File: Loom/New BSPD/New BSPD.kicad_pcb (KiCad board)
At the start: 2 copper layers, 46 parts, among them J1 Conn_01x03, J2 Conn_01x03, J3 Conn_01x03, J4 Screw_Terminal_01x02, K1 MCCMA51-S-DC12V-C, Q1 IRLZ44Z, U1 4011, U10 LM2901, U11 4012, U12 74LS573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

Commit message: Fix bug in state machine counters
Realised that the reset counter would count even in an error
condition, meaning that if 10 seconds pass after shutdown, it will
turn back on instantly after the system is ok.

Fixed by making the reset counter only count if system_ok is high
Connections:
- U1 pad 11: (no net) -> Net-(U1-Pad11)
- U1 pad 12: (no net) -> /System_OK
- U1 pad 13: (no net) -> /State Machine/State_B
- U3 pad 11: (no net) -> Net-(U3-Pad11)
- U3 pad 12: (no net) -> Net-(U1-Pad11)
- U3 pad 13: (no net) -> Net-(U1-Pad11)
- U3 pad 6: /State Machine/State_B -> Net-(U3-Pad11)
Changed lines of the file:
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@@
   (net 112 "unconnected-(U15-Q7-Pad13)")
   (net 113 "unconnected-(U15-Q10-Pad15)")
+  (net 114 "Net-(U1-Pad11)")
+  (net 115 "Net-(U3-Pad11)")
   (footprint "LED_THT:LED_D5.0mm" (layer "F.Cu")
     (at 133.39 80.715)
@@
       (net 38 "Net-(U3-Pad3)") (pintype "input"))
     (pad "6" thru_hole oval (at 0 12.7) (size 1.6 1.6) (drill 0.8) (layers "*.Cu" "*.Mask")
-      (net 40 "/State Machine/State_B") (pintype "input"))
+      (net 115 "Net-(U3-Pad11)") (pintype "input"))
     (pad "7" thru_hole oval (at 0 15.24) (size 1.6 1.6) (drill 0.8) (layers "*.Cu" "*.Mask")
       (net 5 "GND") (pinfunction "VSS") (pintype "power_in"))
@@
     (pad "10" thru_hole oval (at 7.62 10.16) (size 1.6 1.6) (drill 0.8) (layers "*.Cu" "*.Mask")
       (net 41 "/State Machine/Timers/Reset_Counting") (pintype "output"))
-    (pad "11" thru_hole oval (at 7.62 7.62) (size 1.6 1.6) (drill 0.8) (layers "*.Cu" "*.Mask"))
-    (pad "12" thru_hole oval (at 7.62 5.08) (size 1.6 1.6) (drill 0.8) (layers "*.Cu" "*.Mask"))
-    (pad "13" thru_hole oval (at 7.62 2.54) (size 1.6 1.6) (drill 0.8) (layers "*.Cu" "*.Mask"))
+    (pad "11" thru_hole oval (at 7.62 7.62) (size 1.6 1.6) (drill 0.8) (layers "*.Cu" "*.Mask")
+      (net 115 "Net-(U3-Pad11)") (pintype "output"))
+    (pad "12" thru_hole oval (at 7.62 5.08) (size 1.6 1.6) (drill 0.8) (layers "*.Cu" "*.Mask")
+      (net 114 "Net-(U1-Pad11)") (pintype "input"))
+    (pad "13" thru_hole oval (at 7.62 2.54) (size 1.6 1.6) (drill 0.8) (layers "*.Cu" "*.Mask")
+      (net 114 "Net-(U1-Pad11)") (pintype "input"))
     (pad "14" thru_hole oval (at 7.62 0) (size 1.6 1.6) (drill 0.8) (layers "*.Cu" "*.Mask")
       (net 1 "+5V") (pinfunction "VDD") (pintype "power_in"))
@@
     (pad "10" thru_hole oval (at 7.62 10.16) (size 1.6 1.6) (drill 0.8) (layers "*.Cu" "*.Mask")
       (net 33 "/System_OK") (pintype "output"))
-    (pad "11" thru_hole oval (at 7.62 7.62) (size 1.6 1.6) (drill 0.8) (layers "*.Cu" "*.Mask"))
-    (pad "12" thru_hole oval (at 7.62 5.08) (size 1.6 1.6) (drill 0.8) (layers "*.Cu" "*.Mask"))
-    (pad "13" thru_hole oval (at 7.62 2.54) (size 1.6 1.6) (drill 0.8) (layers "*.Cu" "*.Mask"))
+    (pad "11" thru_hole oval (at 7.62 7.62) (size 1.6 1.6) (drill 0.8) (layers "*.Cu" "*.Mask")
+      (net 114 "Net-(U1-Pad11)") (pintype "output"))
+    (pad "12" thru_hole oval (at 7.62 5.08) (size 1.6 1.6) (drill 0.8) (layers "*.Cu" "*.Mask")
+      (net 33 "/System_OK") (pintype "input"))
+    (pad "13" thru_hole oval (at 7.62 2.54) (size 1.6 1.6) (drill 0.8) (layers "*.Cu" "*.Mask")
+      (net 40 "/State Machine/State_B") (pintype "input"))
     (pad "14" thru_hole oval (at 7.62 0) (size 1.6 1.6) (drill 0.8) (layers "*.Cu" "*.Mask")
       (net 1 "+5V") (pinfunction "VDD") (pintype "power_in"))

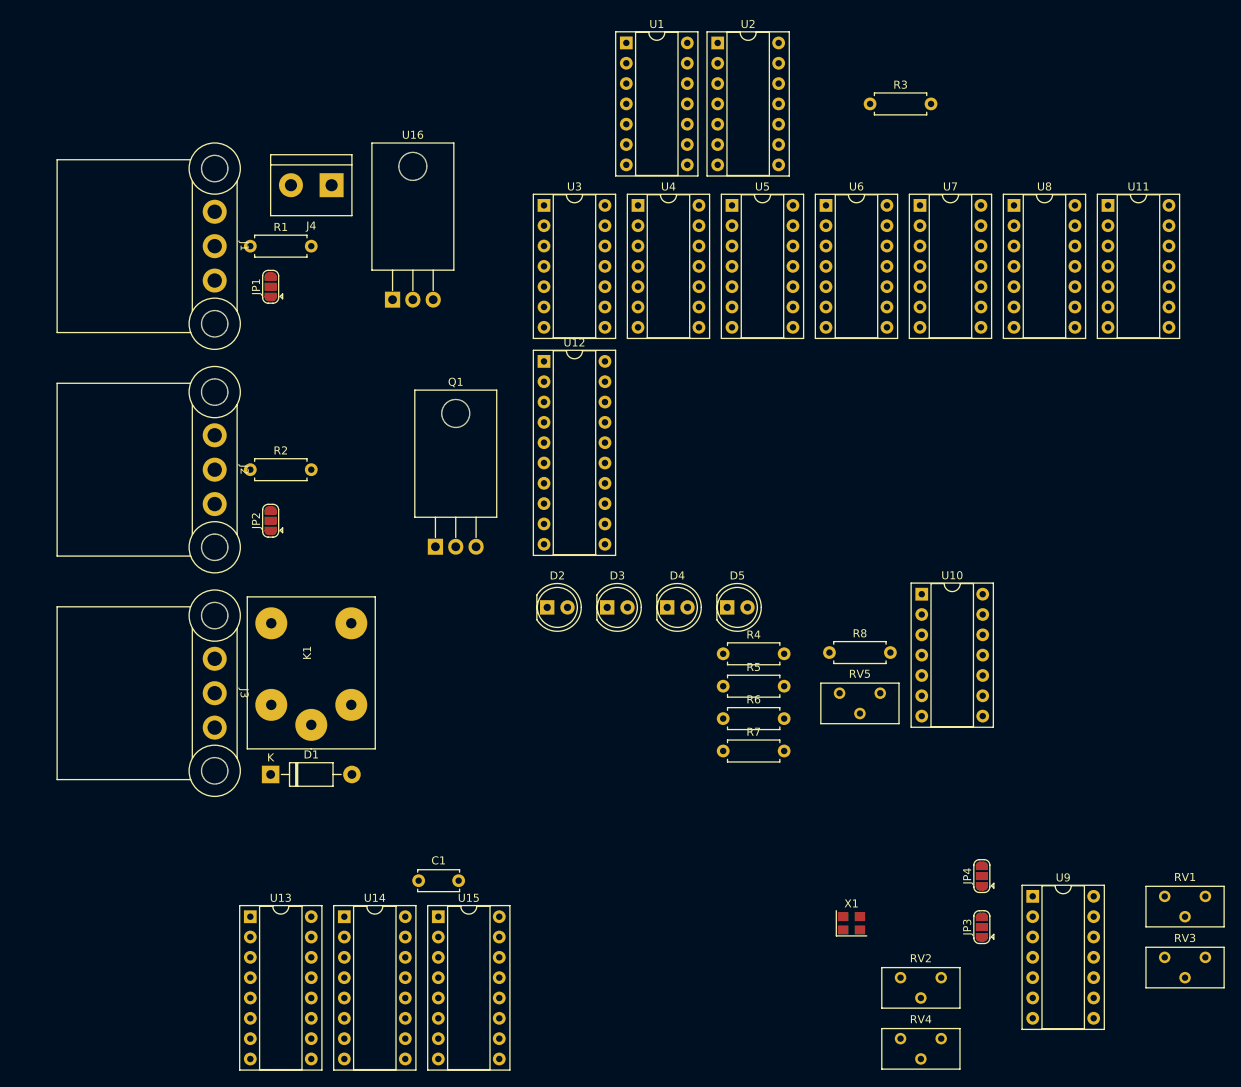
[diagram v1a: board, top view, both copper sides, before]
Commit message: Add State, Shutdown LEDs, Complete rough board layout
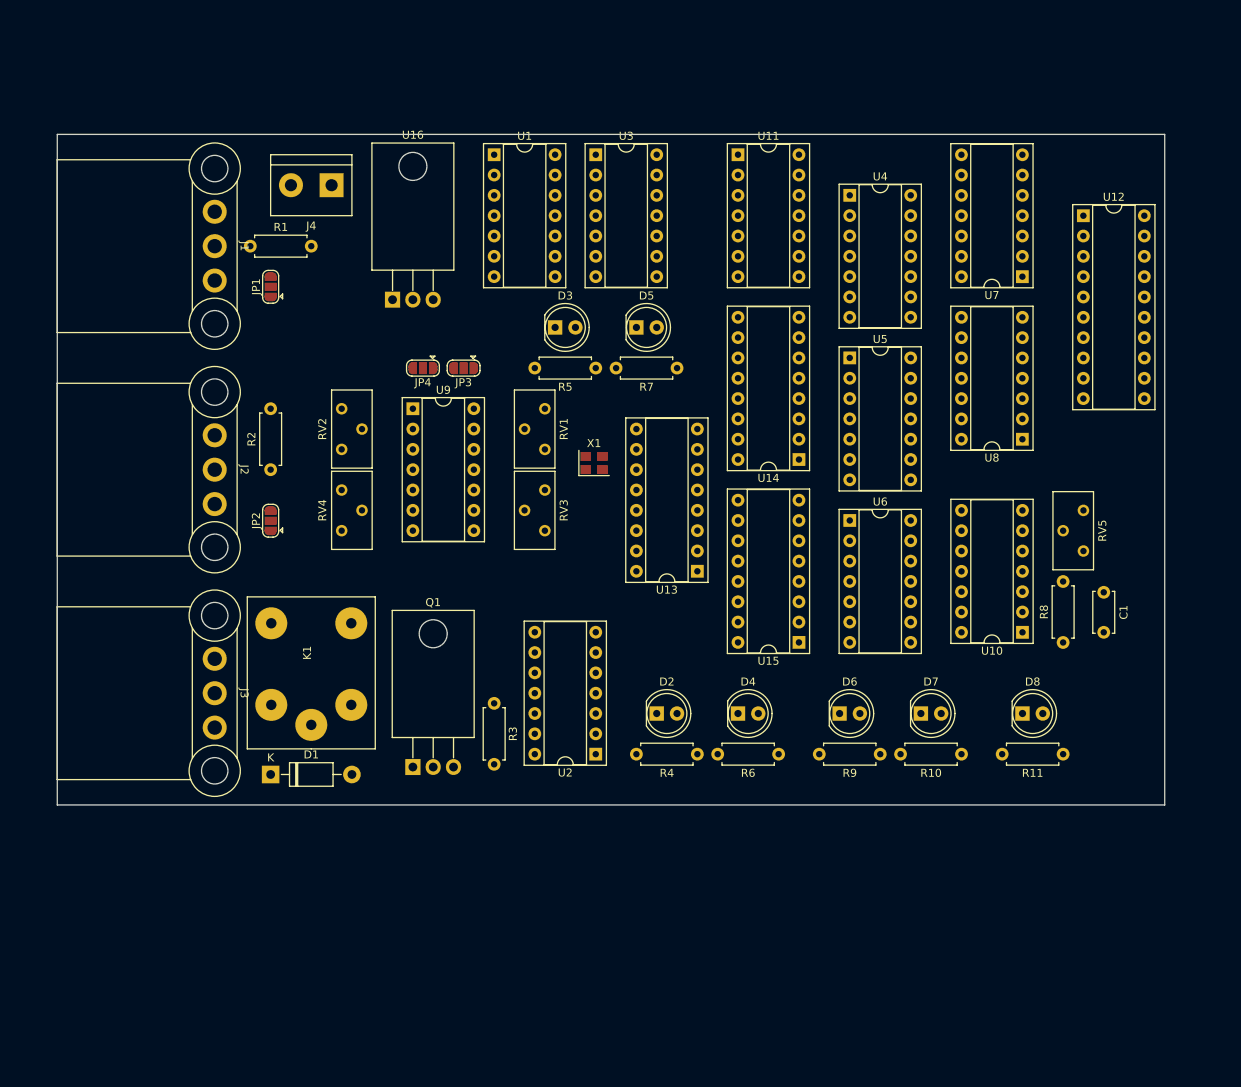
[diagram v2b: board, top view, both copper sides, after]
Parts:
- added D6: LED, LED_THT:LED_D5.0mm, F.Cu at (154.9, 94.0)
- added D7: LED, LED_THT:LED_D5.0mm, F.Cu at (165.1, 94.0)
- added D8: LED, LED_THT:LED_D5.0mm, F.Cu at (177.8, 94.0)
- added R10: 220R, Resistor_THT:R_Axial_DIN0207_L6.3mm_D2.5mm_P7.62mm_Horizontal, F.Cu at (170.2, 99.1)
- added R11: 220R, Resistor_THT:R_Axial_DIN0207_L6.3mm_D2.5mm_P7.62mm_Horizontal, F.Cu at (182.9, 99.1)
- added R9: 220R, Resistor_THT:R_Axial_DIN0207_L6.3mm_D2.5mm_P7.62mm_Horizontal, F.Cu at (160.0, 99.1)
- moved RV2 103.3 mm to (92.7, 55.9), turned to 90 degrees
- moved RV4 101.6 mm to (92.7, 66.0), turned to 90 degrees
- moved RV1 99.7 mm to (118.1, 61.0), turned to -90 degrees
- moved U9 98.6 mm to (101.6, 55.9)
- moved RV3 98.3 mm to (118.1, 71.1), turned to -90 degrees
- moved JP3 95.3 mm to (107.9, 50.8), turned to 180 degrees
- moved JP4 94.4 mm to (102.9, 50.8), turned to 180 degrees
- moved C1 92.9 mm to (188.0, 78.8), turned to -90 degrees
- moved U2 90.2 mm to (124.5, 99.1), turned to 180 degrees
- moved R3 88.4 mm to (111.8, 92.7), turned to -90 degrees
- moved U14 80.6 mm to (149.9, 62.2), turned to 180 degrees
- moved U13 70.6 mm to (137.2, 76.2), turned to 180 degrees
- moved U12 69.8 mm to (185.4, 31.8)
- moved X1 65.9 mm to (124.2, 62.7)
- moved U15 56.6 mm to (149.9, 85.1), turned to 180 degrees
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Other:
- board outline added: 138.4 x 83.8 mm

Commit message: Complete New BSPD!
TODO: Decide if the crystal needs a capacitor or not
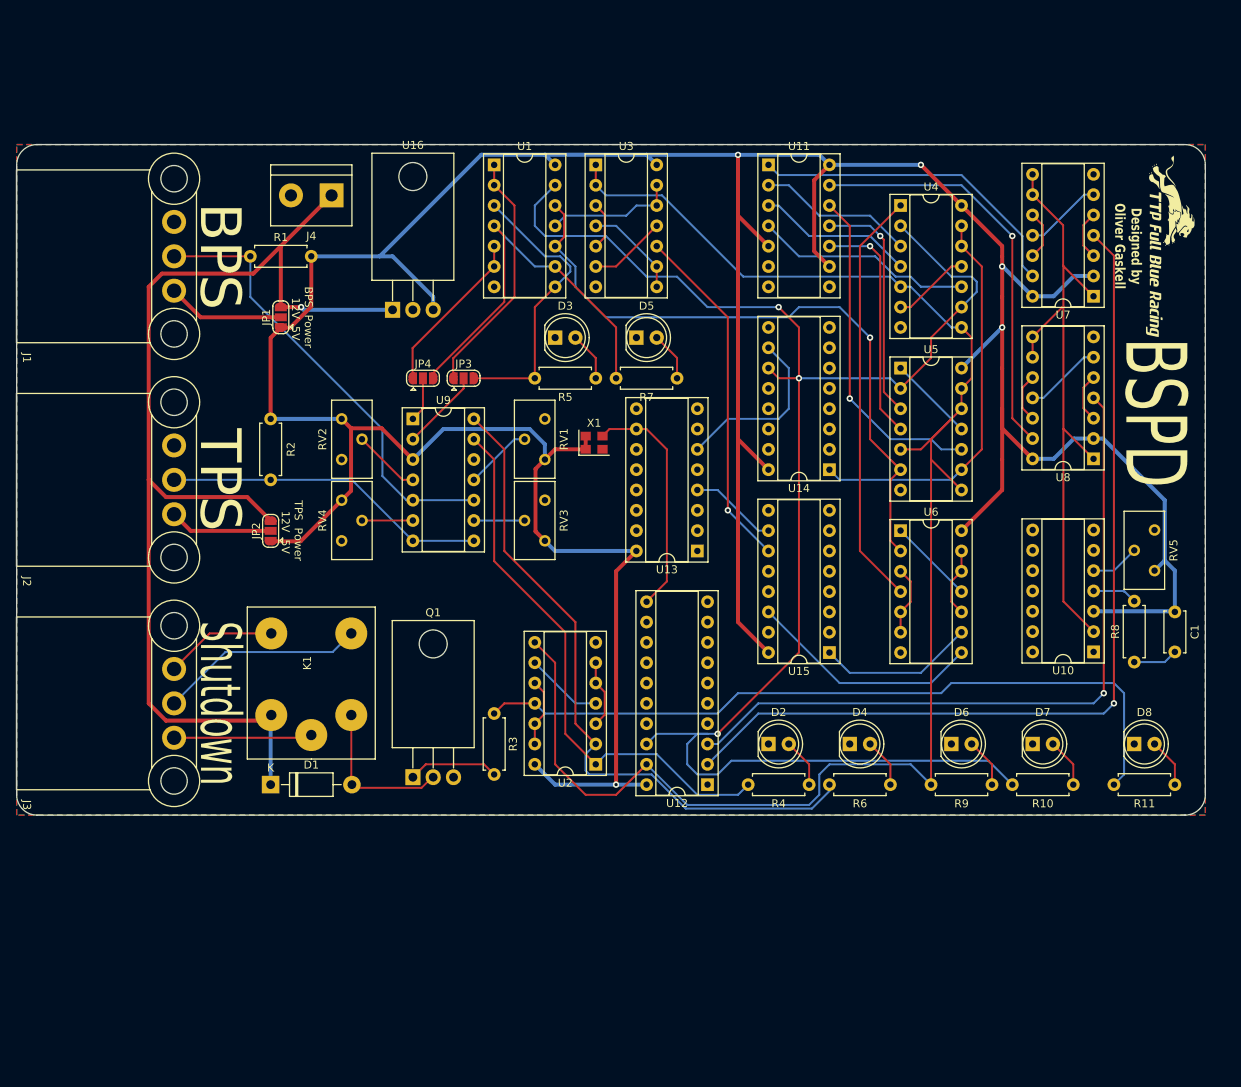
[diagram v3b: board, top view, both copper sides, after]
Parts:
- added G***: LOGO, BSPD_footprints:FBR_Logo_.9in, F.Cu at (196.8, 35.6)
- moved U12 85.2 mm to (138.4, 102.9), turned to 180 degrees
- moved D2 14.5 mm to (146.1, 97.8)
- moved D4 14.5 mm to (156.2, 97.8)
- moved D6 14.5 mm to (168.9, 97.8)
- moved D7 14.5 mm to (179.1, 97.8)
- moved D8 14.5 mm to (191.8, 97.8)
- moved R10 14.5 mm to (184.2, 102.9)
- moved R11 14.5 mm to (196.8, 102.9)
- moved R4 14.5 mm to (151.1, 102.9)
- moved R6 14.5 mm to (161.3, 102.9)
- moved R9 14.5 mm to (174.0, 102.9)
- moved R8 9.22 mm to (191.8, 87.5)
- moved RV5 9.22 mm to (194.3, 76.1)
- moved U7 9.22 mm to (186.7, 41.8)
- moved U8 9.22 mm to (186.7, 62.1)
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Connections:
- U5 pad 3: Net-(U11-Pad10) -> Net-(U11-Pad11)
- U5 pad 4: Net-(U11-Pad11) -> Net-(U11-Pad10)
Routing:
- net +5V: track 0.00 -> 474.3 mm, vias 0 -> 5
- net /State Machine/State_B: track 0.00 -> 204.8 mm, vias 0 -> 3
- net /SM_Ok: track 0.00 -> 201.9 mm
- net +12V: track 0.00 -> 144.5 mm, vias 0 -> 1
- net Net-(U12-D0): track 0.00 -> 113.5 mm, vias 0 -> 1
- net /SD_Sig: track 0.00 -> 93.9 mm
- net Net-(U12-D1): track 0.00 -> 89.6 mm, vias 0 -> 1
- net /TPS_Plugged: track 0.00 -> 85.0 mm
- net /System_OK: track 0.00 -> 82.0 mm, vias 0 -> 1
- net /RST: track 0.00 -> 78.9 mm
- net /BPS_Plugged: track 0.00 -> 69.2 mm
- net /BPS_Sig: track 0.00 -> 56.5 mm
- net Net-(U4-Pad1): track 0.00 -> 52.5 mm
- net Net-(U11-Pad13): track 0.00 -> 51.9 mm, vias 0 -> 1
- net /State Machine/5T: track 0.00 -> 50.2 mm
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- added copper zone on B.Cu, net GND
- added copper zone on F.Cu, net GND
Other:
- board size 138.4 x 83.8 mm -> 148.6 x 83.8 mm
- board text added: "BPS"
- board text added: "BPS Power 12V 5V"
- board text added: "BSPD"
- board text added: "Designed by Oliver Gaskell"
- board text added: "Shutdown"
- board text added: "TPS"
- board text added: "TPS Power 12V 5V"

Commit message: Complete Silkscreen, Fix DRC errors, Misc Cleanup
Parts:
- moved J4 3.59 mm to (88.9, 26.7)
- moved JP3 2.58 mm to (110.5, 52.1)
- moved JP4 2.50 mm to (100.4, 52.1)
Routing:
- net /BPS_Trig: track 36.1 -> 33.5 mm
- net Net-(JP3-C): track 10.2 -> 12.5 mm
- net Net-(JP3-A): track 30.9 -> 29.1 mm
- net /TPS_Trig: track 50.1 -> 51.8 mm
- net +12V: track 144.5 -> 146.0 mm
- net /SM_Ok: track 201.9 -> 203.0 mm
- net Net-(JP4-A): track 20.7 -> 21.8 mm
- net GND: vias 0 -> 24
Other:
- board text added: "12V"
- board text added: "BPS Conn"
- board text added: "BPS Trig"
- board text added: "GND"
- board text added: "System OK"
- board text added: "TPS Conn"
- board text added: "TPS Trig"

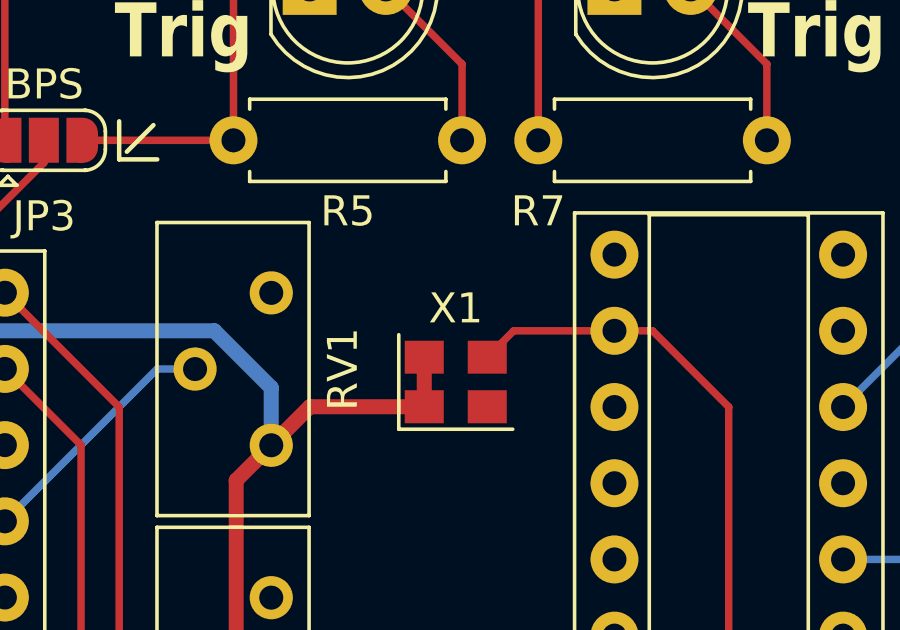
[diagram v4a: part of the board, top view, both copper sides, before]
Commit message: Add filtering capacitor for crystal power
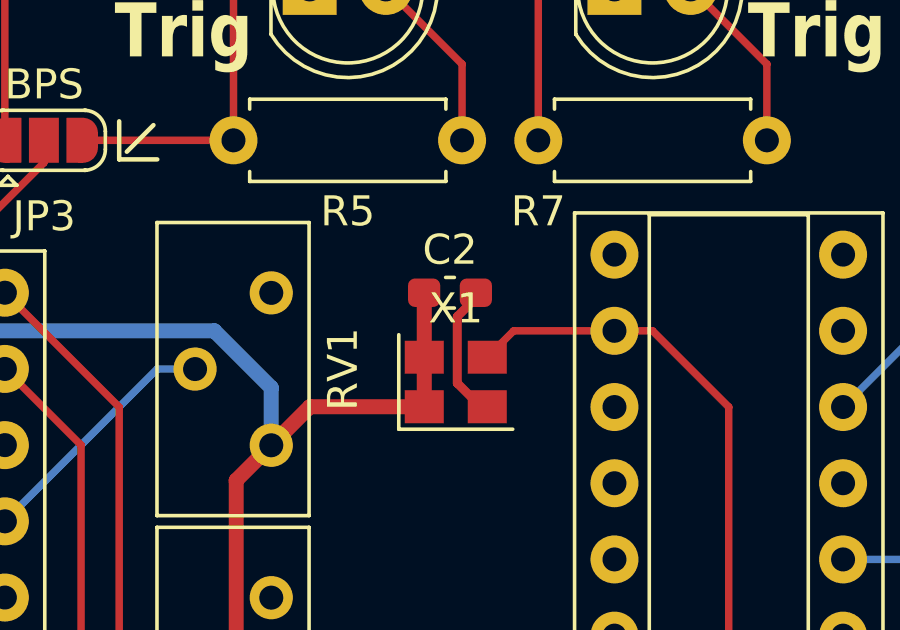
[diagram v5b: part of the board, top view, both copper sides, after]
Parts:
- added C2: 10u, Capacitor_SMD:C_0603_1608Metric_Pad1.08x0.95mm_HandSolder, F.Cu at (124.1, 57.1)
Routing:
- net GND: track 0.00 -> 4.60 mm
- net +5V: track 474.3 -> 476.5 mm
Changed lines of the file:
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@@
     )
   )
+  (footprint "Capacitor_SMD:C_0603_1608Metric_Pad1.08x0.95mm_HandSolder" (layer "F.Cu")
+    (at 124.0575 57.15)
+    (descr "Capacitor SMD 0603 (1608 Metric), square (rectangular) end terminal, IPC_7351 nominal with elongated pad for handsoldering. (Body size source: IPC-SM-782 page 76, https://www.pcb-3d.com/wordpress/wp-content/uploads/ipc-sm-782a_amendment_1_and_2.pdf), generated with kicad-footprint-generator")
+    (tags "capacitor handsolder")
+    (property "Sheetfile" "New BSPD.kicad_sch")
+    (property "Sheetname" "")
+    (property "ki_description" "Unpolarized capacitor")
+    (property "ki_keywords" "cap capacitor")
+    (attr smd)
+    (fp_text reference "C2" (at 0 -1.43) (layer "F.SilkS")
+        (effects (font (size 1 1) (thickness 0.15)))
+    )
+    (fp_text value "10u" (at 0 1.43) (layer "F.Fab")
+        (effects (font (size 1 1) (thickness 0.15)))
+    )
+    (fp_text user "${REFERENCE}" (at 0 0) (layer "F.Fab")
+        (effects (font (size 0.4 0.4) (thickness 0.06)))
+    )
+    (fp_line (start -0.146267 -0.51) (end 0.146267 -0.51)
+      (stroke (width 0.12) (type solid)) (layer "F.SilkS"))
+    (fp_line (start -0.146267 0.51) (end 0.146267 0.51)
+      (stroke (width 0.12) (type solid)) (layer "F.SilkS"))
+    (fp_line (start -1.65 -0.73) (end 1.65 -0.73)
+      (stroke (width 0.05) (type solid)) (layer "F.CrtYd"))
+    (fp_line (start -1.65 0.73) (end -1.65 -0.73)
+      (stroke (width 0.05) (type solid)) (layer "F.CrtYd"))
+    (fp_line (start 1.65 -0.73) (end 1.65 0.73)
+      (stroke (width 0.05) (type solid)) (layer "F.CrtYd"))
+    (fp_line (start 1.65 0.73) (end -1.65 0.73)
+      (stroke (width 0.05) (type solid)) (layer "F.CrtYd"))
+    (fp_line (start -0.8 -0.4) (end 0.8 -0.4)
+      (stroke (width 0.1) (type solid)) (layer "F.Fab"))
+    (fp_line (start -0.8 0.4) (end -0.8 -0.4)
+      (stroke (width 0.1) (type solid)) (layer "F.Fab"))
+    (fp_line (start 0.8 -0.4) (end 0.8 0.4)
+      (stroke (width 0.1) (type solid)) (layer "F.Fab"))
+    (fp_line (start 0.8 0.4) (end -0.8 0.4)
+      (stroke (width 0.1) (type solid)) (layer "F.Fab"))
+    (pad "1" smd roundrect (at -0.8625 0) (size 1.075 0.95) (layers "F.Cu" "F.Paste" "F.Mask") (roundrect_rratio 0.25)
+      (net 1 "+5V") (pintype "passive"))
+    (pad "2" smd roundrect (at 0.8625 0) (size 1.075 0.95) (layers "F.Cu" "F.Paste" "F.Mask") (roundrect_rratio 0.25)
+      (net 5 "GND") (pintype "passive"))
+    (model "${KICAD6_3DMODEL_DIR}/Capacitor_SMD.3dshapes/C_0603_1608Metric.wrl"
+      (offset (xyz 0 0 0))
+      (scale (xyz 1 1 1))
+      (rotate (xyz 0 0 0))
+    )
+  )
   (footprint "LED_THT:LED_D5.0mm" (layer "F.Cu")
     (at 168.91 97.79)
@@
   (segment (start 86.262082 45.75) (end 88.9 43.112082) (width 0.5) (layer "F.Cu") (net 1))
   (segment (start 142.24 82.55) (end 146.05 86.36) (width 0.5) (layer "F.Cu") (net 1))
+  (segment (start 123.2 59.3) (end 123.2 57.155) (width 0.5) (layer "F.Cu") (net 1))
   (segment (start 153.67 25.4) (end 151.765 27.305) (width 0.5) (layer "F.Cu") (net 1))
   (segment (start 175.26 50.8) (end 175.26 55.88) (width 0.5) (layer "F.Cu") (net 1))
@@
   (segment (start 146.05 35.56) (end 142.24 31.75) (width 0.5) (layer "F.Cu") (net 1))
   (segment (start 85.09 45.75) (end 83.82 47.02) (width 0.5) (layer "F.Cu") (net 1))
+  (segment (start 123.2 57.155) (end 123.195 57.15) (width 0.5) (layer "F.Cu") (net 1))
   (segment (start 175.26 35.555) (end 175.26 36.83) (width 0.5) (layer "F.Cu") (net 1))
   (segment (start 116.93 71.225) (end 116.93 63.405) (width 0.5) (layer "F.Cu") (net 1))
@@
   (segment (start 93.9 102.79) (end 93.98 102.87) (width 0.25) (layer "F.Cu") (net 4))
   (segment (start 93.9 94.17) (end 93.9 102.79) (width 0.25) (layer "F.Cu") (net 4))
+  (segment (start 124.3 57.945) (end 124.3 60.165) (width 0.3) (layer "F.Cu") (net 5))
+  (segment (start 124.92 57.15) (end 124.92 57.325) (width 0.5) (layer "F.Cu") (net 5))
+  (segment (start 124.3 60.165) (end 125.085 60.95) (width 0.3) (layer "F.Cu") (net 5))
+  (segment (start 124.92 57.325) (end 124.3 57.945) (width 0.3) (layer "F.Cu") (net 5))
+  (segment (start 125.085 60.95) (end 125.3 60.95) (width 0.3) (layer "F.Cu") (net 5))
   (via (at 158.75 41.275) (size 0.8) (drill 0.4) (layers "F.Cu" "B.Cu") (free) (net 5))
   (via (at 121.285 99.695) (size 0.8) (drill 0.4) (layers "F.Cu" "B.Cu") (free) (net 5))
